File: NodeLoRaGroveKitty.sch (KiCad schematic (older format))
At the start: 39 parts, among them P1 PICKIT PROGRAMMER, P2 Battery, P3 A0, P4 D9, P5 USB-Serial, P6 I2C, SW1 SW_BOOT, SW2 SW_RESET, U1 AP2112, U2 MCP73831T-2ATI/OT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

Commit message: Update BOM
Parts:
- C4, C5: manf# (none) -> GRM21BR71E104KA01L
- D2, D3, D4: manf# (none) -> 859-LTST-C170KRKT
- P3, P4, P6: manf# (none) -> S4B-PH-K-S(LF)(SN)
- R10, R14, R8: manf# AC0805KRX7R7BB104 -> WR08X1003FTL
- R11: manf# (none) -> AF0805FR-0710KL
- R2: manf# (none) -> WR08X1003FTL
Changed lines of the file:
@@
 F 2 "Connectors_JST:JST_PH_S4B-PH-K_04x2.00mm_Angled" H 10950 5250 50  0001 C CNN
 F 3 "" H 10950 5250 50  0000 C CNN
+F 4 "S4B-PH-K-S(LF)(SN)" H 10950 5250 60  0001 C CNN "manf#"
 	1    10950 5250
 	1    0    0    -1
@@
 F 2 "Resistors_SMD:R_0805_HandSoldering" H 1450 6300 50  0001 C CNN
 F 3 "" H 1450 6300 50  0000 C CNN
+F 4 "WR08X1003FTL" H 1450 6300 60  0001 C CNN "manf#"
 	1    1450 6300
 	0    1    1    0
@@
 F 2 "Resistors_SMD:R_0805_HandSoldering" H 6050 6300 50  0001 C CNN
 F 3 "" H 6050 6300 50  0000 C CNN
+F 4 "AF0805FR-0710KL" H 6050 6300 60  0001 C CNN "manf#"
 	1    6050 6300
 	1    0    0    -1
@@
 F 2 "LEDs:LED_0805" V 3700 6200 50  0001 C CNN
 F 3 "" V 3700 6200 50  0000 C CNN
+F 4 "859-LTST-C170KRKT" H 3700 6200 60  0001 C CNN "manf#"
 	1    3700 6200
 	-1   0    0    1
@@
 F 2 "LEDs:LED_0805" V 3700 6500 50  0001 C CNN
 F 3 "" V 3700 6500 50  0000 C CNN
+F 4 "859-LTST-C170KRKT" H 3700 6500 60  0001 C CNN "manf#"
 	1    3700 6500
 	1    0    0    -1
@@
 F 2 "Connectors_JST:JST_PH_S4B-PH-K_04x2.00mm_Angled" H 9750 5250 50  0001 C CNN
 F 3 "" H 9750 5250 50  0000 C CNN
+F 4 "S4B-PH-K-S(LF)(SN)" H 9750 5250 60  0001 C CNN "manf#"
 	1    9750 5250
 	1    0    0    -1
@@
 F 2 "Connectors_JST:JST_PH_S4B-PH-K_04x2.00mm_Angled" H 9750 6250 50  0001 C CNN
 F 3 "" H 9750 6250 50  0000 C CNN
+F 4 "S4B-PH-K-S(LF)(SN)" H 9750 6250 60  0001 C CNN "manf#"
 	1    9750 6250
 	1    0    0    -1
@@
 F 2 "Capacitors_SMD:C_0805_HandSoldering" H 3450 1050 50  0001 C CNN
 F 3 "" H 3450 1050 50  0000 C CNN
+F 4 "GRM21BR71E104KA01L" H 3450 1050 60  0001 C CNN "manf#"
 	1    3450 1050
 	1    0    0    -1
@@
 F 2 "LEDs:LED_0805" V 1200 2550 50  0001 C CNN
 F 3 "" V 1200 2550 50  0000 C CNN
+F 4 "859-LTST-C170KRKT" H 1200 2550 60  0001 C CNN "manf#"
 	1    1200 2550
 	0    -1   -1   0
@@
 F 2 "Capacitors_SMD:C_0805_HandSoldering" H 3850 1050 50  0001 C CNN
 F 3 "" H 3850 1050 50  0000 C CNN
+F 4 "GRM21BR71E104KA01L" H 3850 1050 60  0001 C CNN "manf#"
 	1    3850 1050
 	1    0    0    -1
@@
 F 2 "Resistors_SMD:R_0805_HandSoldering" V 4830 3870 50  0001 C CNN
 F 3 "" H 4900 3870 50  0000 C CNN
-F 4 "AC0805KRX7R7BB104" V 4900 3870 60  0001 C CNN "manf#"
+F 4 "WR08X1003FTL" V 4900 3870 60  0001 C CNN "manf#"
 	1    4900 3870
 	0    1    1    0
@@
 F 2 "Resistors_SMD:R_0805_HandSoldering" V 5250 3870 50  0001 C CNN
 F 3 "" H 5320 3870 50  0000 C CNN
-F 4 "AC0805KRX7R7BB104" V 5320 3870 60  0001 C CNN "manf#"
+F 4 "WR08X1003FTL" V 5320 3870 60  0001 C CNN "manf#"
 	1    5320 3870
 	0    1    1    0
@@
 F 2 "Resistors_SMD:R_0805_HandSoldering" V 5810 3870 50  0001 C CNN
 F 3 "" H 5880 3870 50  0000 C CNN
-F 4 "AC0805KRX7R7BB104" V 5880 3870 60  0001 C CNN "manf#"
+F 4 "WR08X1003FTL" V 5880 3870 60  0001 C CNN "manf#"
 	1    5880 3870
 	0    1    1    0

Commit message: Change to AP2114
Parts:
- removed C3: 1uF, Capacitors_SMD:C_0805_HandSoldering, symbol C_Small
- C1, C2: value 10uF -> 4.7uF
- U1: value AP2112 -> AP2114; footprint TO_SOT_Packages_SMD:SOT-23-5 -> TO_SOT_Packages_SMD:SOT-223; manf# AP2112K-3.3TRG1 -> AP2114H-3.3TRG1

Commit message: Add mbr120
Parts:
- added D?: MBR120, Diodes_SMD:SOD-123, symbol ZENERsmall
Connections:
- net VCC: now also D?.2 (A); no longer C1.1, D1.1 (K), R2.2, U1.3 (IN)
- new net: C1.1, D1.1 (K), D?.1 (K), R2.2, U1.3 (IN)
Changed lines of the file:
@@
 	1    0    0    -1
+$EndComp
+$Comp
+L ZENERsmall D?
+U 1 1 58924335
+P 595 5845
+F 0 "D?" H 595 5645 50  0000 C CNN
+F 1 "MBR120" H 600 5930 50  0000 C CNN
+F 2 "Diodes_SMD:SOD-123" H 595 5845 50  0001 C CNN
+F 3 "" H 595 5845 50  0000 C CNN
+F 4 "NRVB120VLSFT1G" H 595 5845 60  0001 C CNN "manf#"
+	1    595  5845
+	0    -1   -1   0
 $EndComp
 Wire Wire Line
@@
 	2900 6100 2900 6000
 Connection ~ 700  6100
-Wire Wire Line
-	600  5550 600  6100
 Connection ~ 1000 6450
 Wire Wire Line
@@
 Wire Wire Line
 	2600 6100 2900 6100
+Wire Wire Line
+	595  5745 595  5550
+Wire Wire Line
+	595  5550 600  5550
+Wire Wire Line
+	600  6100 600  5945
+Wire Wire Line
+	600  5945 595  5945
 $EndSCHEMATC

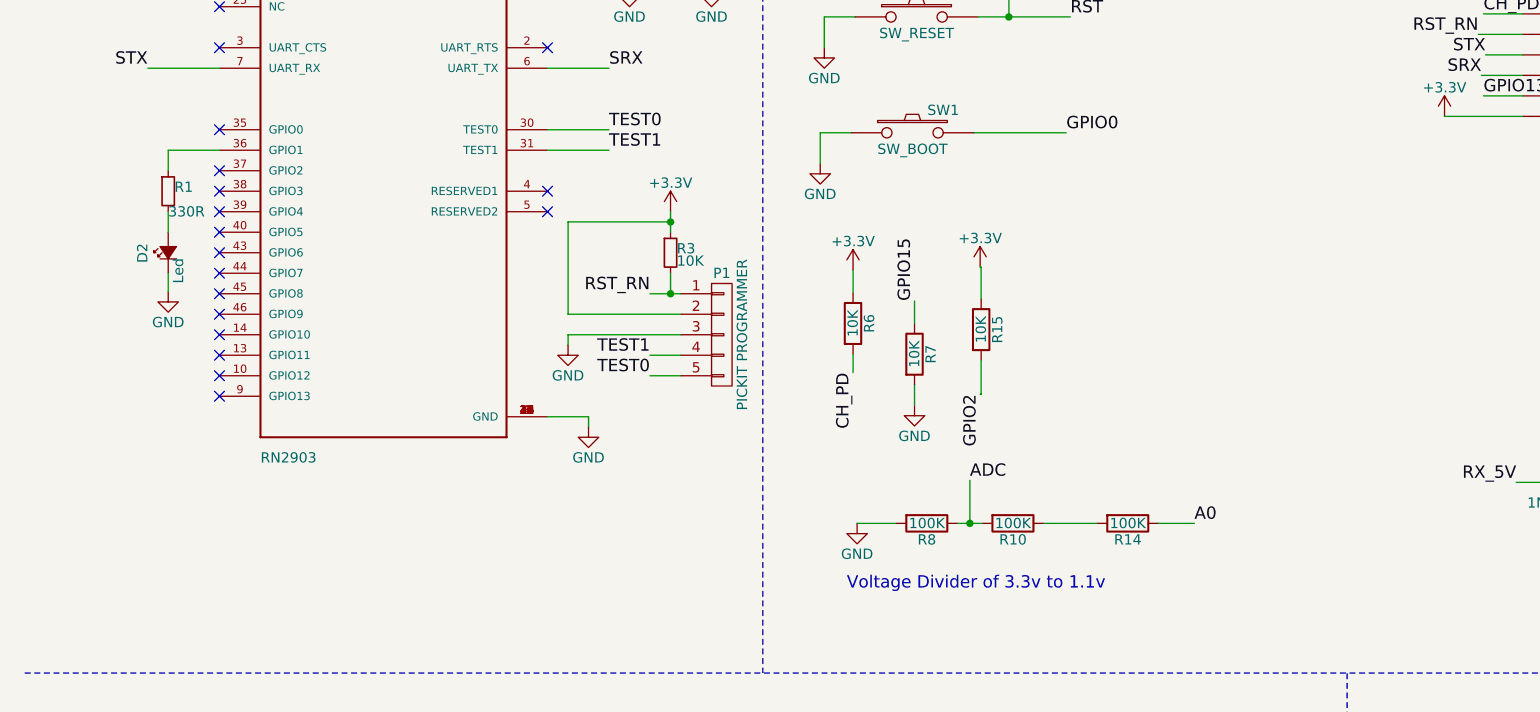
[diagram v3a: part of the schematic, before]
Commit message: Change Led to GPIO0
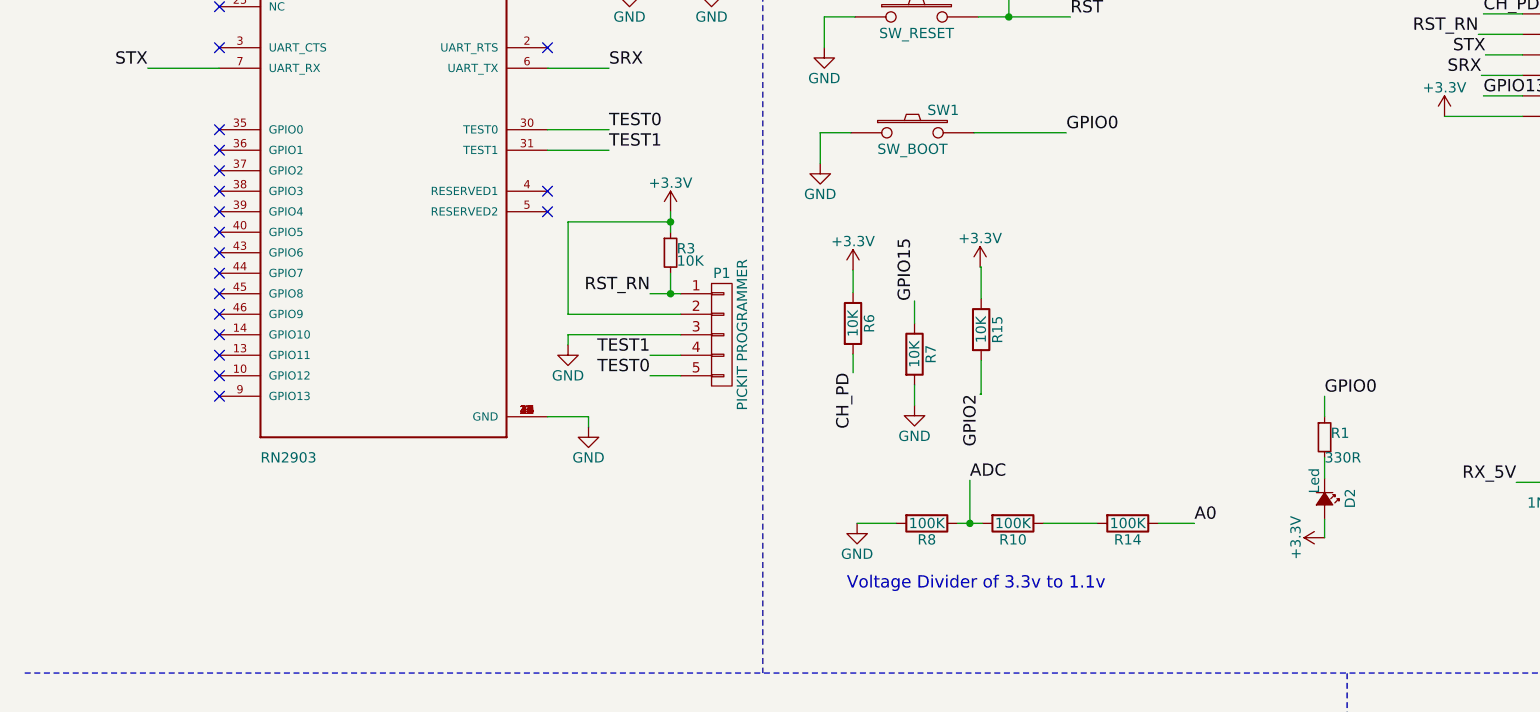
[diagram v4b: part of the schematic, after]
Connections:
- net +3V3: now also D2.2 (A)
- net GND: no longer D2.1 (K)
- net GPIO0: now also R1.1
- net at MODULE1.36 (GPIO1): no longer R1.1
- net at R1.2: now also D2.1 (K); no longer D2.2 (A)
- no-connect marks 28 -> 29
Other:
- moved on the sheet: D2, R1
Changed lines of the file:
@@
-	1    0    0    -1
-$EndComp
-$Comp
-L R_Small R1
-U 1 1 57D2387F
-P 1200 2250
-F 0 "R1" H 1230 2270 50  0000 L CNN
-F 1 "330R" H 1200 2150 50  0000 L CNN
-F 2 "Resistors_SMD:R_0805_HandSoldering" H 1200 2250 50  0001 C CNN
-F 3 "" H 1200 2250 50  0000 C CNN
-F 4 "ERJ-6GEYJ331V" H 1200 2250 60  0001 C CNN "manf#"
-	1    1200 2250
-	1    0    0    -1
-$EndComp
-$Comp
-L Led_Small D2
-U 1 1 57D23DF7
-P 1200 2550
-F 0 "D2" H 1150 2675 50  0000 L CNN
-F 1 "Led" H 1050 2500 50  0000 L CNN
-F 2 "LEDs:LED_0805" V 1200 2550 50  0001 C CNN
-F 3 "" V 1200 2550 50  0000 C CNN
-F 4 "859-LTST-C170KRKT" H 1200 2550 60  0001 C CNN "manf#"
-	1    1200 2550
-	0    -1   -1   0
-$EndComp
-$Comp
-L GND #PWR020
-U 1 1 57D24767
-P 1200 2740
-F 0 "#PWR020" H 1200 2490 50  0001 C CNN
-F 1 "GND" H 1200 2590 50  0000 C CNN
-F 2 "" H 1200 2740 50  0000 C CNN
-F 3 "" H 1200 2740 50  0000 C CNN
-	1    1200 2740
 	1    0    0    -1
 $EndComp
@@
 	4540 2745 4540 2635
 Wire Wire Line
-	1200 2650 1200 2740
+	6840 3850 6840 3940
 Wire Wire Line
 	7805 1585 7625 1585
@@
 	3850 1150 3850 1250
 Wire Wire Line
-	1200 2350 1200 2450
-Wire Wire Line
-	1200 2050 1200 2150
+	6840 3550 6840 3650
+Wire Wire Line
+	6840 3250 6840 3350
 Wire Wire Line
 	3450 1150 3450 1250
@@
 	3050 1950 3350 1950
 Wire Wire Line
-	1450 2050 1200 2050
-Wire Wire Line
 	1450 1650 1100 1650
 Wire Wire Line
@@
 Wire Wire Line
 	600  5945 595  5945
+$Comp
+L Led_Small D2
+U 1 1 57D23DF7
+P 6840 3750
+F 0 "D2" H 6790 3875 50  0000 L CNN
+F 1 "Led" H 6690 3700 50  0000 L CNN
+F 2 "LEDs:LED_0805" V 6840 3750 50  0001 C CNN
+F 3 "" V 6840 3750 50  0000 C CNN
+F 4 "859-LTST-C170KRKT" H 6840 3750 60  0001 C CNN "manf#"
+	1    6840 3750
+	0    1    1    0
+$EndComp
+$Comp
+L R_Small R1
+U 1 1 57D2387F
+P 6840 3450
+F 0 "R1" H 6870 3470 50  0000 L CNN
+F 1 "330R" H 6840 3350 50  0000 L CNN
+F 2 "Resistors_SMD:R_0805_HandSoldering" H 6840 3450 50  0001 C CNN
+F 3 "" H 6840 3450 50  0000 C CNN
+F 4 "ERJ-6GEYJ331V" H 6840 3450 60  0001 C CNN "manf#"
+	1    6840 3450
+	1    0    0    -1
+$EndComp
+NoConn ~ 1450 2050
+$Comp
+L +3.3V #PWR?
+U 1 1 58926B64
+P 6840 3940
+F 0 "#PWR?" H 6840 3790 50  0001 C CNN
+F 1 "+3.3V" H 6840 4080 50  0000 C CNN
+F 2 "" H 6840 3940 50  0000 C CNN
+F 3 "" H 6840 3940 50  0000 C CNN
+	1    6840 3940
+	0    -1   -1   0
+$EndComp
+Text Label 6840 3250 0    60   ~ 0
+GPIO0
 $EndSCHEMATC
